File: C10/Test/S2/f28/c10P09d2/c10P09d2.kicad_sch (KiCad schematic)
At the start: 3 parts

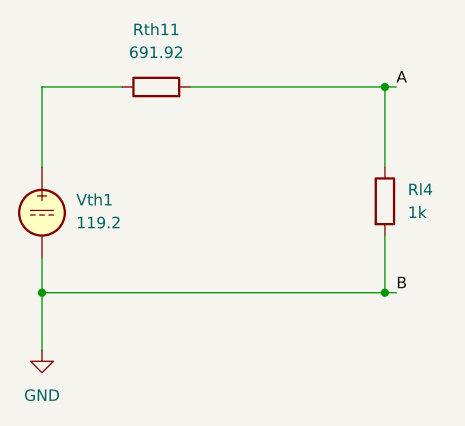
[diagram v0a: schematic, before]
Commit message: corrected from misprinting Fig 10-28
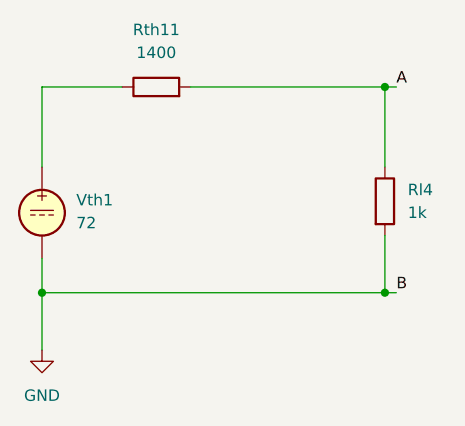
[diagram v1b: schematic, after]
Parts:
- Rth11: value 691.92 -> 1400
- Vth1: value 119.2 -> 72
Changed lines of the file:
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@@
 			)
 		)
-		(property "Value" "119.2"
+		(property "Value" "72"
 			(at 139.7 86.2301 0)
 			(show_name no)
@@
 			)
 		)
-		(property "Value" "691.92"
+		(property "Value" "1400"
 			(at 148.59 67.31 90)
 			(show_name no)
